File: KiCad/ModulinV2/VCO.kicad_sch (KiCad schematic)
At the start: 99 parts, among them Q1 MMBFJ201, Q2 MMBFJ201, SW3 SW_SPDT_MSM, U3 AS3340, U4 AS3340

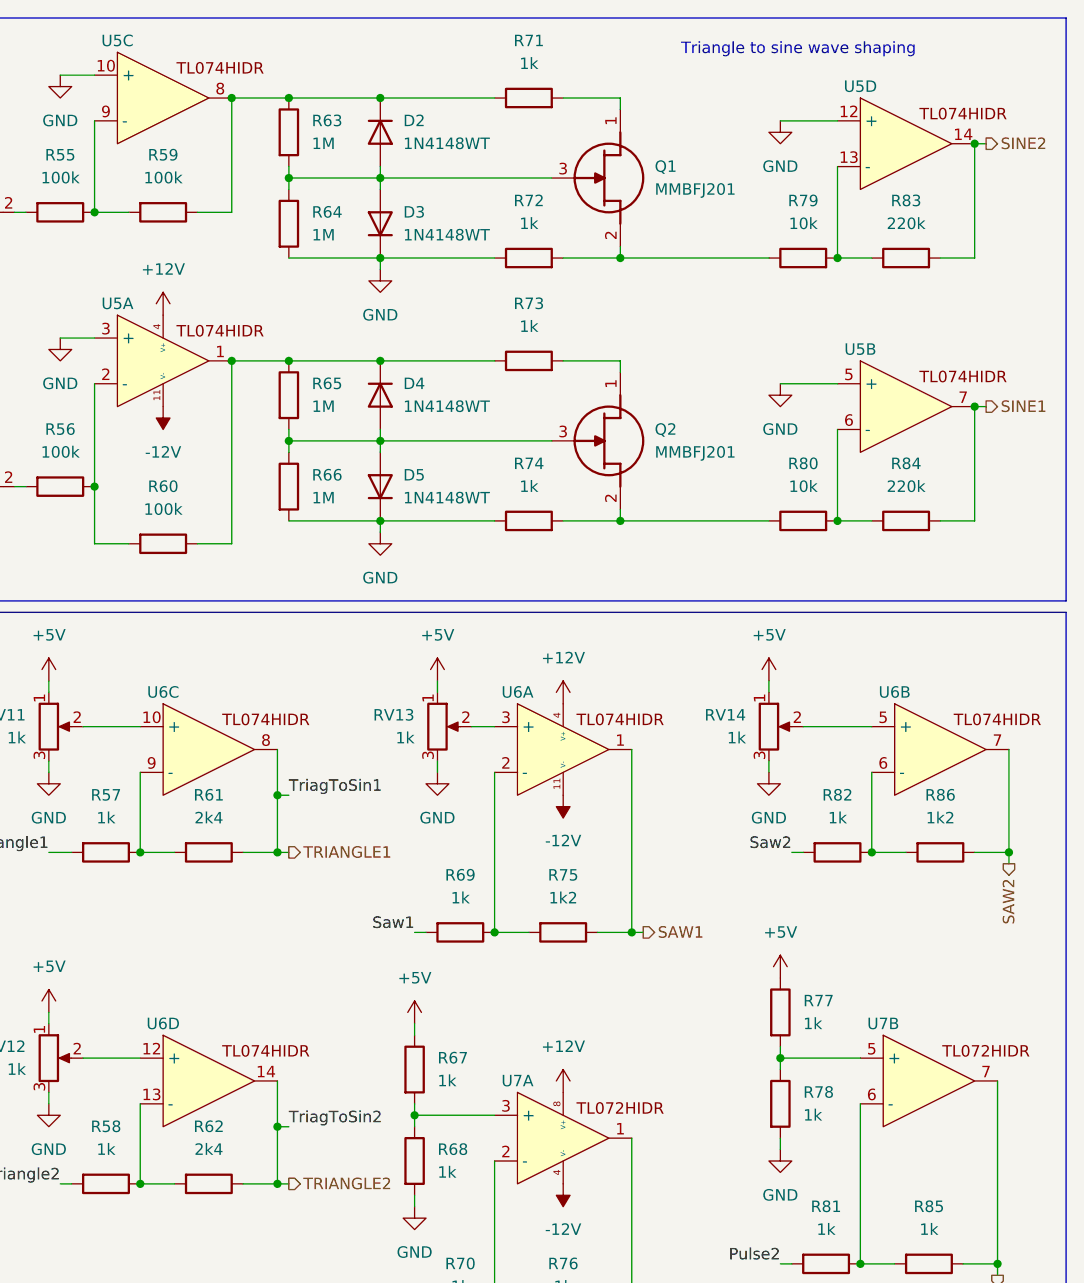
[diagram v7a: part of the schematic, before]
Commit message: Updated TL074 and 72 symbols
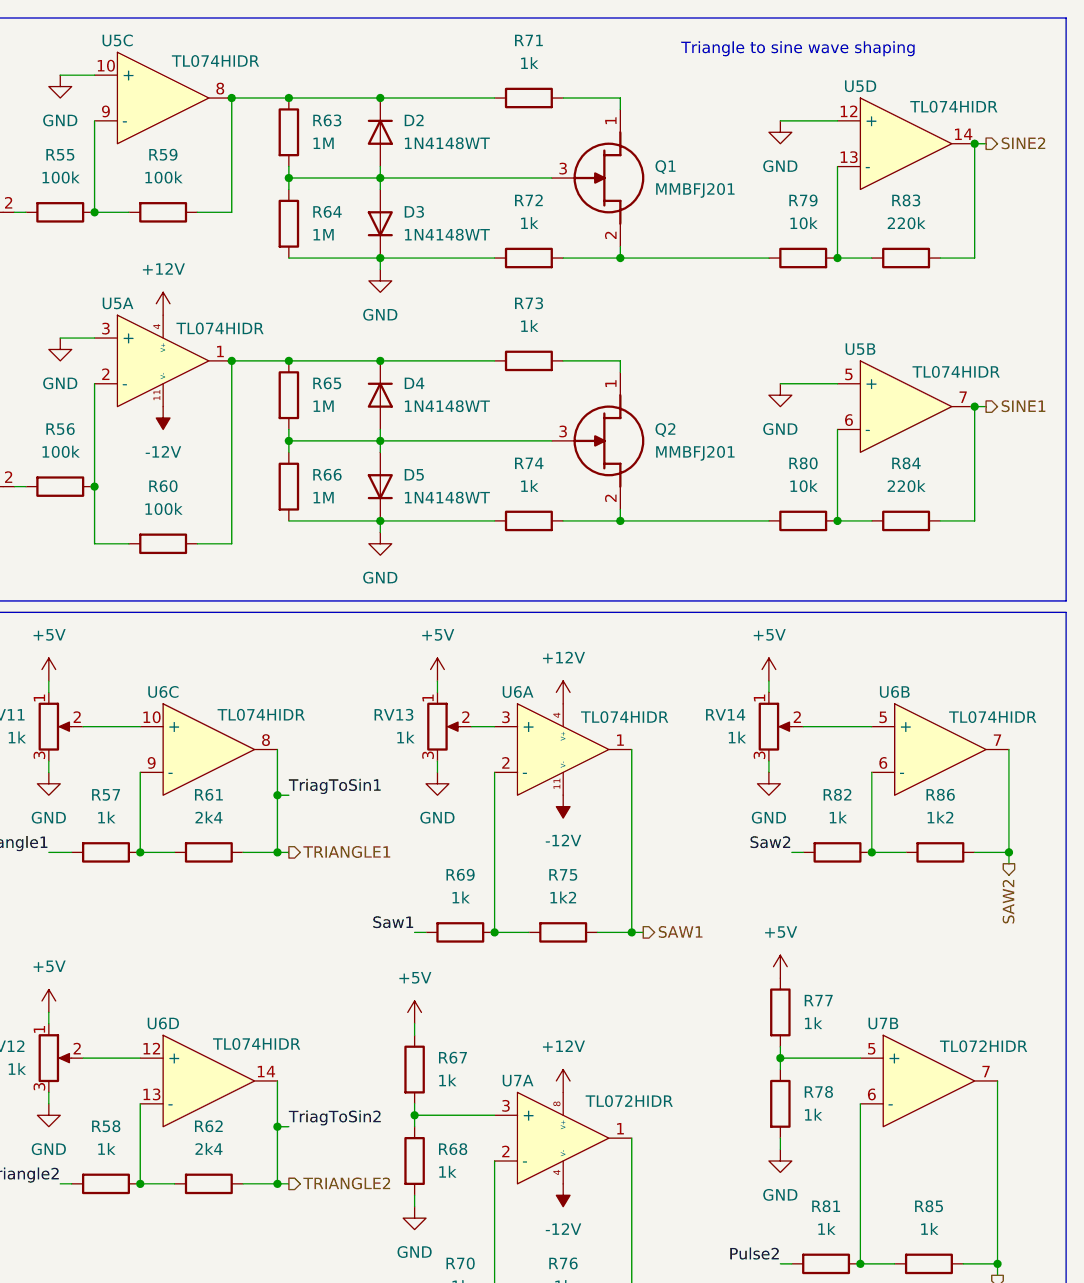
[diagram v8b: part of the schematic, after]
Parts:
- U5, U6: value ~ -> TL074HIDR
- U7: value ~ -> TL072HIDR
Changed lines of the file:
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@@
 		(on_board yes)
 		(dnp no)
-		(fields_autoplaced yes)
 		(property "Reference" "U6"
 			(at 264.16 88.9 0)
@@
 			)
 		)
-		(property "Value" "~"
-			(at 272.4555 88.9 0)
+		(property "Value" "TL074HIDR"
+			(at 275.082 91.694 0)
 			(effects
 				(font
@@
 		(on_board yes)
 		(dnp no)
-		(fields_autoplaced yes)
 		(property "Reference" "U7"
 			(at 222.25 132.08 0)
@@
 			)
 		)
-		(property "Value" "~"
-			(at 240.03 135.1849 0)
+		(property "Value" "TL072HIDR"
+			(at 234.696 134.366 0)
 			(effects
 				(font
@@
 		(on_board yes)
 		(dnp no)
-		(fields_autoplaced yes)
 		(property "Reference" "U6"
 			(at 182.88 88.9 0)
@@
 			)
 		)
-		(property "Value" "~"
-			(at 191.1755 88.9 0)
+		(property "Value" "TL074HIDR"
+			(at 193.802 91.44 0)
 			(effects
 				(font
@@
 		(on_board yes)
 		(dnp no)
-		(fields_autoplaced yes)
 		(property "Reference" "U5"
 			(at 177.8 45.72 0)
@@
 			)
 		)
-		(property "Value" "~"
-			(at 195.58 48.8249 0)
+		(property "Value" "TL074HIDR"
+			(at 189.23 48.514 0)
 			(effects
 				(font
@@
 		(on_board yes)
 		(dnp no)
-		(fields_autoplaced yes)
 		(property "Reference" "U5"
 			(at 260.35 21.59 0)
@@
 			)
 		)
-		(property "Value" "~"
-			(at 268.6455 21.59 0)
+		(property "Value" "TL074HIDR"
+			(at 270.764 23.876 0)
 			(effects
 				(font
@@
 		(on_board yes)
 		(dnp no)
-		(fields_autoplaced yes)
 		(property "Reference" "U6"
 			(at 182.88 125.73 0)
@@
 			)
 		)
-		(property "Value" "~"
-			(at 191.1755 125.73 0)
+		(property "Value" "TL074HIDR"
+			(at 193.294 128.016 0)
 			(effects
 				(font
@@
 		(on_board yes)
 		(dnp no)
-		(fields_autoplaced yes)
 		(property "Reference" "U7"
 			(at 262.89 125.73 0)
@@
 			)
 		)
-		(property "Value" "~"
-			(at 271.1855 125.73 0)
+		(property "Value" "TL072HIDR"
+			(at 274.066 128.27 0)
 			(effects
 				(font
@@
 		(on_board yes)
 		(dnp no)
-		(fields_autoplaced yes)
 		(property "Reference" "U5"
 			(at 260.35 50.8 0)
@@
 			)
 		)
-		(property "Value" "~"
-			(at 268.6455 50.8 0)
+		(property "Value" "TL074HIDR"
+			(at 271.018 53.34 0)
 			(effects
 				(font
@@
 		(on_board yes)
 		(dnp no)
-		(fields_autoplaced yes)
 		(property "Reference" "U6"
 			(at 222.25 88.9 0)
@@
 			)
 		)
-		(property "Value" "~"
-			(at 240.03 92.0049 0)
+		(property "Value" "TL074HIDR"
+			(at 234.188 91.694 0)
 			(effects
 				(font
@@
 		(on_board yes)
 		(dnp no)
-		(fields_autoplaced yes)
 		(property "Reference" "U5"
 			(at 177.8 16.51 0)
@@
 			)
 		)
-		(property "Value" "~"
-			(at 186.0955 16.51 0)
+		(property "Value" "TL074HIDR"
+			(at 188.722 18.796 0)
 			(effects
 				(font
